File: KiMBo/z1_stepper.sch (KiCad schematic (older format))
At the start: 23 parts, among them U17 TMC2130

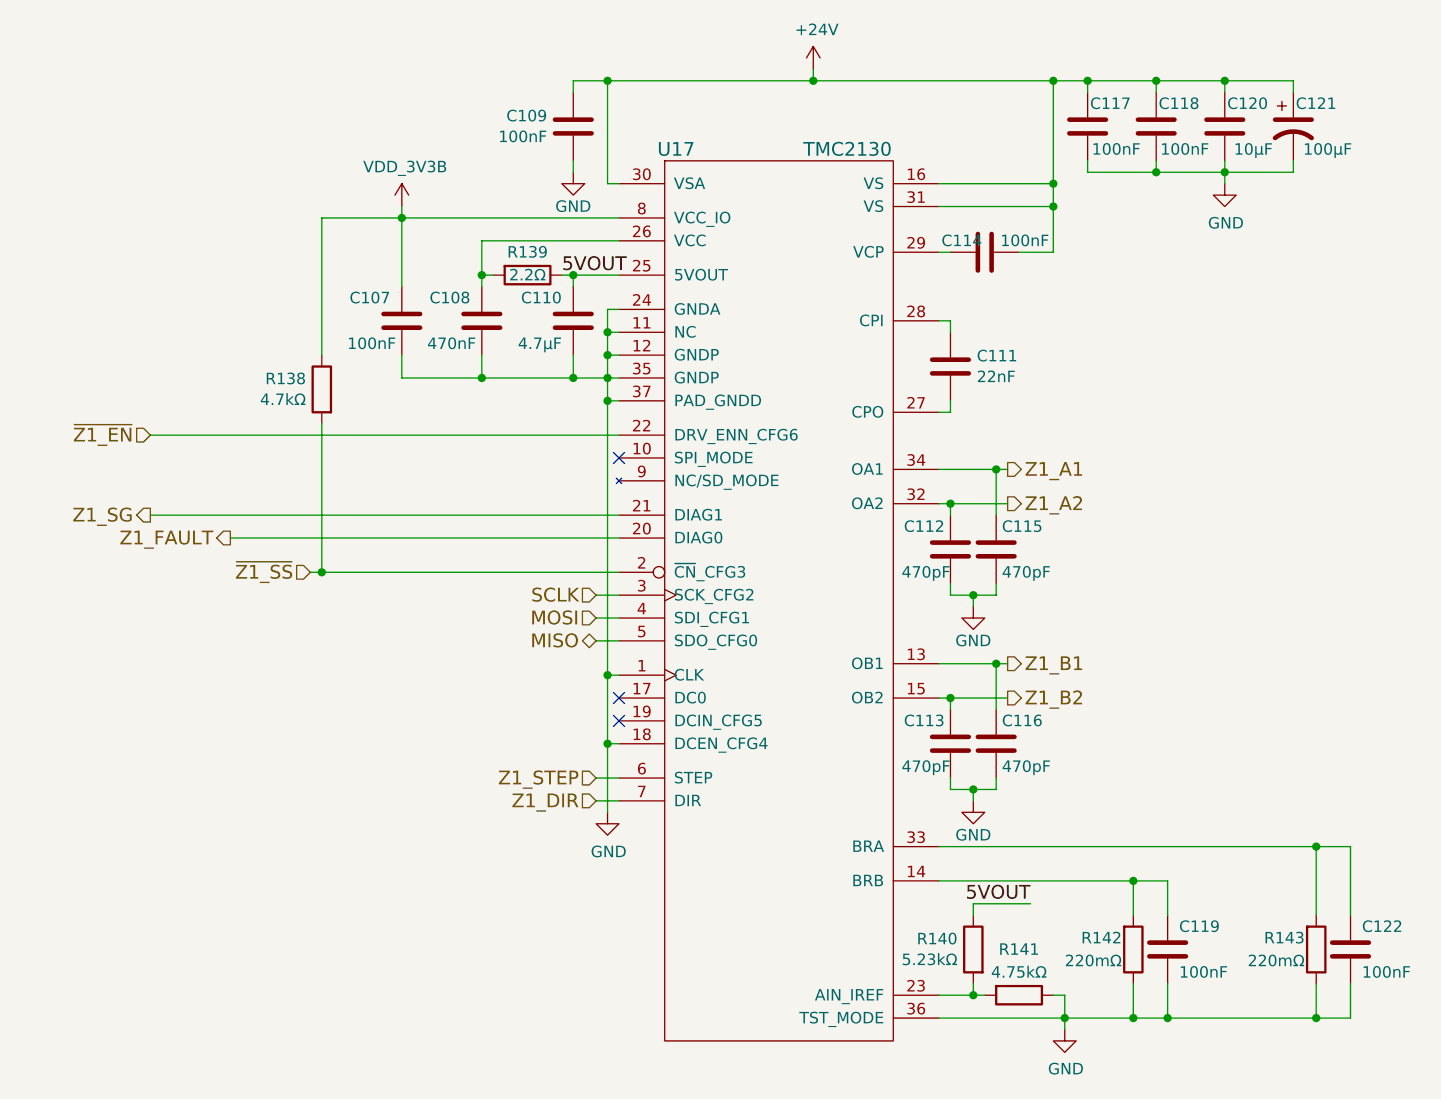
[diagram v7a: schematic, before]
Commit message: Daisy chain the SPI stepper motor driver interface, continue work on the E-heater layout
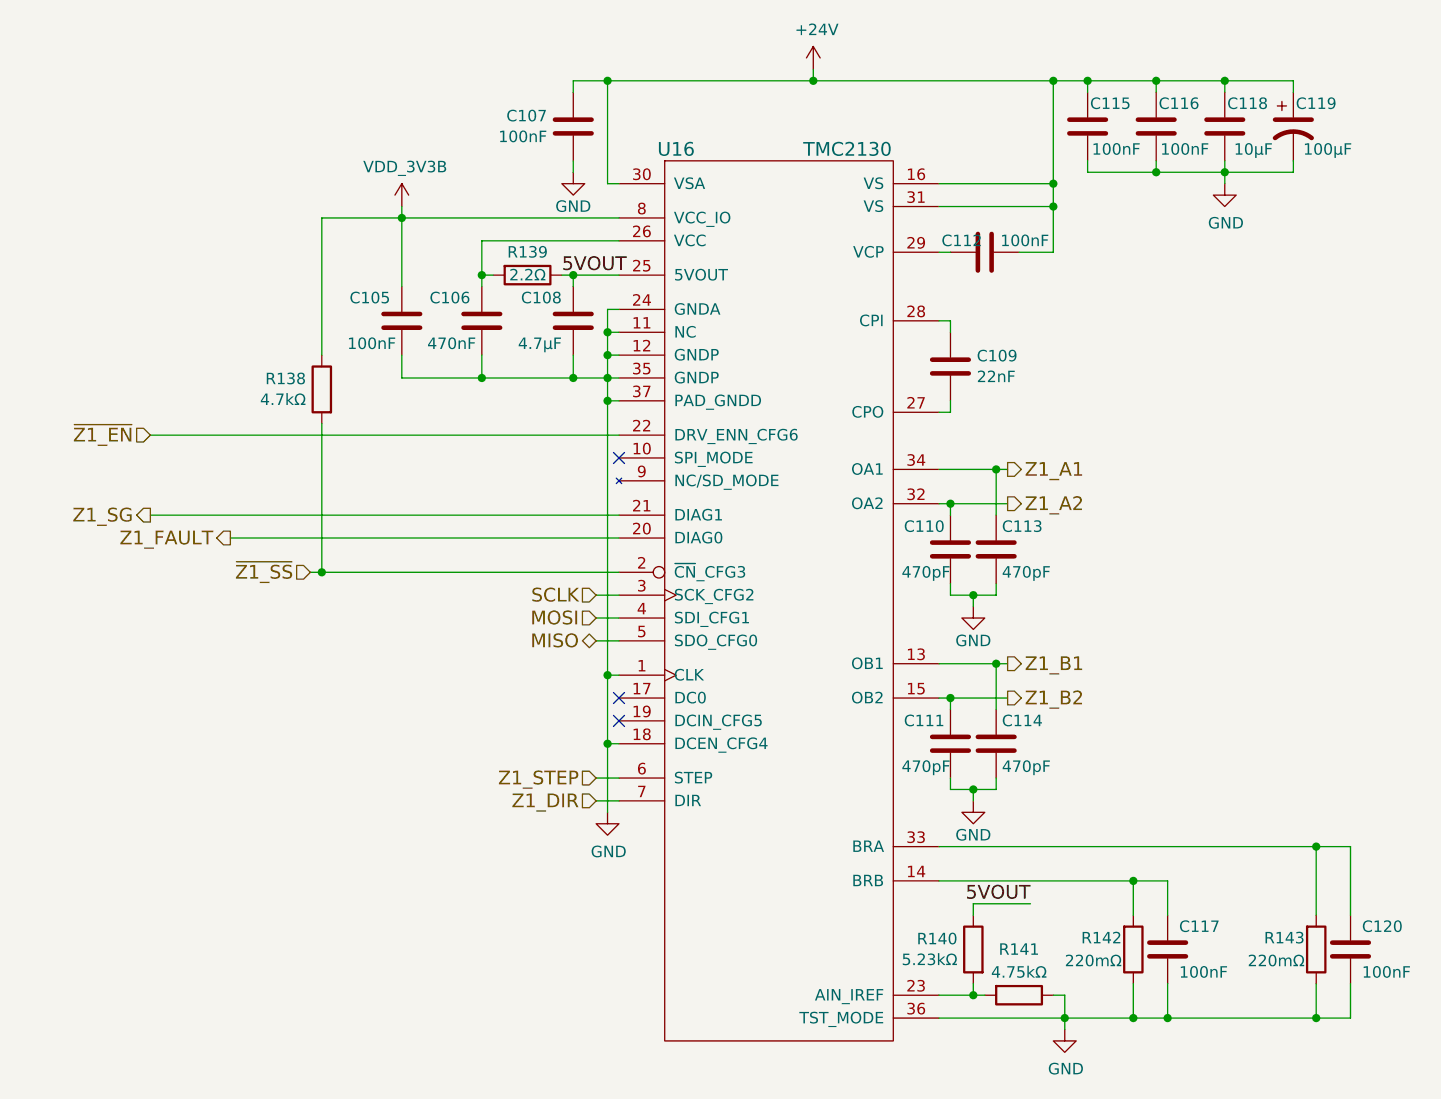
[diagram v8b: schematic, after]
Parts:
- renumbered C107 to C105, C108 to C106, C109 to C107, C110 to C108, C111 to C109, C112 to C110, C113 to C111, C114 to C112, C115 to C113, C116 to C114, C117 to C115, C118 to C116, C119 to C117, C120 to C118, C121 to C119, C122 to C120, U17 to U16
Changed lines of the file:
@@
 Z1_SG
 $Comp
-L C C109
+L C C107
 U 1 1 58C0CFD1
 P 7400 3050
-F 0 "C109" H 7286 3004 50  0000 R CNN
+F 0 "C107" H 7286 3004 50  0000 R CNN
 F 1 "100nF" H 7286 3095 50  0000 R CNN
 F 2 "Capacitors_SMD:C_0603" H 7438 2900 50  0001 C CNN
@@
 $EndComp
 $Comp
-L C C114
+L C C112
 U 1 1 58C0CFD8
 P 9200 3600
-F 0 "C114" V 9150 3500 50  0000 C CNN
+F 0 "C112" V 9150 3500 50  0000 C CNN
 F 1 "100nF" V 9150 3775 50  0000 C CNN
 F 2 "Capacitors_SMD:C_0603" H 9238 3450 50  0001 C CNN
@@
 $EndComp
 $Comp
-L CP1 C121
+L CP1 C119
 U 1 1 58C0CFDF
 P 10550 3050
-F 0 "C121" H 10650 3150 50  0000 C CNN
+F 0 "C119" H 10650 3150 50  0000 C CNN
 F 1 "100μF" H 10700 2950 50  0000 C CNN
 F 2 "Capacitors_SMD:c_elec_8x10" H 10550 3050 50  0001 C CNN
@@
 $EndComp
 $Comp
-L C C117
+L C C115
 U 1 1 58C0CFE6
 P 9650 3050
-F 0 "C117" H 9550 3150 50  0000 C CNN
+F 0 "C115" H 9550 3150 50  0000 C CNN
 F 1 "100nF" H 9525 2950 50  0000 C CNN
 F 2 "Capacitors_SMD:C_0603" H 9688 2900 50  0001 C CNN
@@
 $EndComp
 $Comp
-L GND #PWR0193
+L GND #PWR173
 U 1 1 58C0CFED
 P 7400 3250
-F 0 "#PWR0193" H 7400 3000 50  0001 C CNN
+F 0 "#PWR173" H 7400 3000 50  0001 C CNN
 F 1 "GND" H 7400 3100 50  0000 C CNN
 F 2 "" H 7400 3250 50  0000 C CNN
@@
 $EndComp
 $Comp
-L C C118
+L C C116
 U 1 1 58C0CFF3
 P 9950 3050
-F 0 "C118" H 9850 3150 50  0000 C CNN
+F 0 "C116" H 9850 3150 50  0000 C CNN
 F 1 "100nF" H 9825 2950 50  0000 C CNN
 F 2 "Capacitors_SMD:C_0603" H 9988 2900 50  0001 C CNN
@@
 $EndComp
 $Comp
-L GND #PWR0194
+L GND #PWR179
 U 1 1 58C0CFFA
 P 10250 3300
-F 0 "#PWR0194" H 10250 3050 50  0001 C CNN
+F 0 "#PWR179" H 10250 3050 50  0001 C CNN
 F 1 "GND" H 10255 3127 50  0000 C CNN
 F 2 "" H 10250 3300 50  0000 C CNN
@@
 $EndComp
 $Comp
-L +24V #PWR0195
+L +24V #PWR175
 U 1 1 58C0D000
 P 8450 2800
-F 0 "#PWR0195" H 8450 2650 50  0001 C CNN
+F 0 "#PWR175" H 8450 2650 50  0001 C CNN
 F 1 "+24V" H 8465 2973 50  0000 C CNN
 F 2 "" H 8450 2800 50  0000 C CNN
@@
 $EndComp
 $Comp
-L C C111
+L C C109
 U 1 1 58C0D006
 P 9050 4100
-F 0 "C111" H 9165 4146 50  0000 L CNN
+F 0 "C109" H 9165 4146 50  0000 L CNN
 F 1 "22nF" H 9165 4055 50  0000 L CNN
 F 2 "Capacitors_SMD:C_0603" H 9088 3950 50  0001 C CNN
@@
 $EndComp
 $Comp
-L GND #PWR0196
+L GND #PWR178
 U 1 1 58C0D01B
 P 9550 7000
-F 0 "#PWR0196" H 9550 6750 50  0001 C CNN
+F 0 "#PWR178" H 9550 6750 50  0001 C CNN
 F 1 "GND" H 9555 6827 50  0000 C CNN
 F 2 "" H 9550 7000 50  0000 C CNN
@@
 $EndComp
 $Comp
-L C C108
+L C C106
 U 1 1 58C0D029
 P 7000 3900
-F 0 "C108" H 7050 4000 50  0000 L CNN
+F 0 "C106" H 7050 4000 50  0000 L CNN
 F 1 "470nF" H 7025 3800 50  0000 L CNN
 F 2 "Capacitors_SMD:C_0603" H 7038 3750 50  0001 C CNN
@@
 NoConn ~ 7600 5650
 $Comp
-L GND #PWR0197
+L GND #PWR174
 U 1 1 58C0D03E
 P 7550 6050
-F 0 "#PWR0197" H 7550 5800 50  0001 C CNN
+F 0 "#PWR174" H 7550 5800 50  0001 C CNN
 F 1 "GND" H 7555 5877 50  0000 C CNN
 F 2 "" H 7550 6050 50  0000 C CNN
@@
 $EndComp
 $Comp
-L C C119
+L C C117
 U 1 1 58C0D044
 P 10000 6650
-F 0 "C119" H 10050 6750 50  0000 L CNN
+F 0 "C117" H 10050 6750 50  0000 L CNN
 F 1 "100nF" H 10050 6550 50  0000 L CNN
 F 2 "Capacitors_SMD:C_0603" H 10038 6500 50  0001 C CNN
@@
 NoConn ~ 7600 4500
 $Comp
-L C C110
+L C C108
 U 1 1 58C0D056
 P 7400 3900
-F 0 "C110" H 7450 4000 50  0000 L CNN
+F 0 "C108" H 7450 4000 50  0000 L CNN
 F 1 "4.7μF" H 7450 3800 50  0000 L CNN
 F 2 "Capacitors_SMD:C_0603" H 7438 3750 50  0001 C CNN
@@
 $EndComp
 $Comp
-L C C122
+L C C120
 U 1 1 58C0D074
 P 10800 6650
-F 0 "C122" H 10850 6750 50  0000 L CNN
+F 0 "C120" H 10850 6750 50  0000 L CNN
 F 1 "100nF" H 10850 6550 50  0000 L CNN
 F 2 "Capacitors_SMD:C_0603" H 10838 6500 50  0001 C CNN
@@
 $EndComp
 $Comp
-L C C112
+L C C110
 U 1 1 58C0D07B
 P 9050 4900
-F 0 "C112" H 9075 5000 50  0000 L CNN
+F 0 "C110" H 9075 5000 50  0000 L CNN
 F 1 "470pF" H 9050 4800 50  0000 L CNN
 F 2 "Capacitors_SMD:C_0603" H 9088 4750 50  0001 C CNN
@@
 $EndComp
 $Comp
-L GND #PWR0198
+L GND #PWR176
 U 1 1 58C0D082
 P 9150 5150
-F 0 "#PWR0198" H 9150 4900 50  0001 C CNN
+F 0 "#PWR176" H 9150 4900 50  0001 C CNN
 F 1 "GND" H 9150 5000 50  0000 C CNN
 F 2 "" H 9150 5150 50  0000 C CNN
@@
 $EndComp
 $Comp
-L C C115
+L C C113
 U 1 1 58C0D088
 P 9250 4900
-F 0 "C115" H 9275 5000 50  0000 L CNN
+F 0 "C113" H 9275 5000 50  0000 L CNN
 F 1 "470pF" H 9275 4800 50  0000 L CNN
 F 2 "Capacitors_SMD:C_0603" H 9288 4750 50  0001 C CNN
@@
 $EndComp
 $Comp
-L C C113
+L C C111
 U 1 1 58C0D08F
 P 9050 5750
-F 0 "C113" H 9075 5850 50  0000 L CNN
+F 0 "C111" H 9075 5850 50  0000 L CNN
 F 1 "470pF" H 9050 5650 50  0000 L CNN
 F 2 "Capacitors_SMD:C_0603" H 9088 5600 50  0001 C CNN
@@
 $EndComp
 $Comp
-L GND #PWR0199
+L GND #PWR177
 U 1 1 58C0D096
 P 9150 6000
-F 0 "#PWR0199" H 9150 5750 50  0001 C CNN
+F 0 "#PWR177" H 9150 5750 50  0001 C CNN
 F 1 "GND" H 9150 5850 50  0000 C CNN
 F 2 "" H 9150 6000 50  0000 C CNN
@@
 $EndComp
 $Comp
-L C C116
+L C C114
 U 1 1 58C0D09C
 P 9250 5750
-F 0 "C116" H 9275 5850 50  0000 L CNN
+F 0 "C114" H 9275 5850 50  0000 L CNN
 F 1 "470pF" H 9275 5650 50  0000 L CNN
 F 2 "Capacitors_SMD:C_0603" H 9288 5600 50  0001 C CNN
@@
 $EndComp
 $Comp
-L TMC2130 U17
+L TMC2130 U16
 U 1 1 58C0D0A3
 P 8300 4650
-F 0 "U17" H 7850 6150 60  0000 C CNN
+F 0 "U16" H 7850 6150 60  0000 C CNN
 F 1 "TMC2130" H 8600 6150 60  0000 C CNN
 F 2 "KiMBo:QFN36_5X6" H 8300 4950 60  0001 C CNN
@@
 	9050 5950 9050 5900
 $Comp
-L C C120
+L C C118
 U 1 1 58C0D122
 P 10250 3050
-F 0 "C120" H 10150 3150 50  0000 C CNN
+F 0 "C118" H 10150 3150 50  0000 C CNN
 F 1 "10μF" H 10125 2950 50  0000 C CNN
 F 2 "Capacitors_SMD:C_0805" H 10288 2900 50  0001 C CNN
@@
 	9000 4550 9300 4550
 $Comp
-L VDD_3V3B #PWR0200
+L VDD_3V3B #PWR172
 U 1 1 5A314607
 P 6650 3400
-F 0 "#PWR0200" H 6650 3250 50  0001 C CNN
+F 0 "#PWR172" H 6650 3250 50  0001 C CNN
 F 1 "VDD_3V3B" H 6665 3573 50  0000 C CNN
 F 2 "" H 6650 3400 50  0000 C CNN
@@
 $EndComp
 $Comp
-L C C107
+L C C105
 U 1 1 5A89C1CC
 P 6650 3900
-F 0 "C107" H 6700 4000 50  0000 L CNN
+F 0 "C105" H 6700 4000 50  0000 L CNN
 F 1 "100nF" H 6675 3800 50  0000 L CNN
 F 2 "Capacitors_SMD:C_0603" H 6688 3750 50  0001 C CNN
